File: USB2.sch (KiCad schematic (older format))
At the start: 21 parts

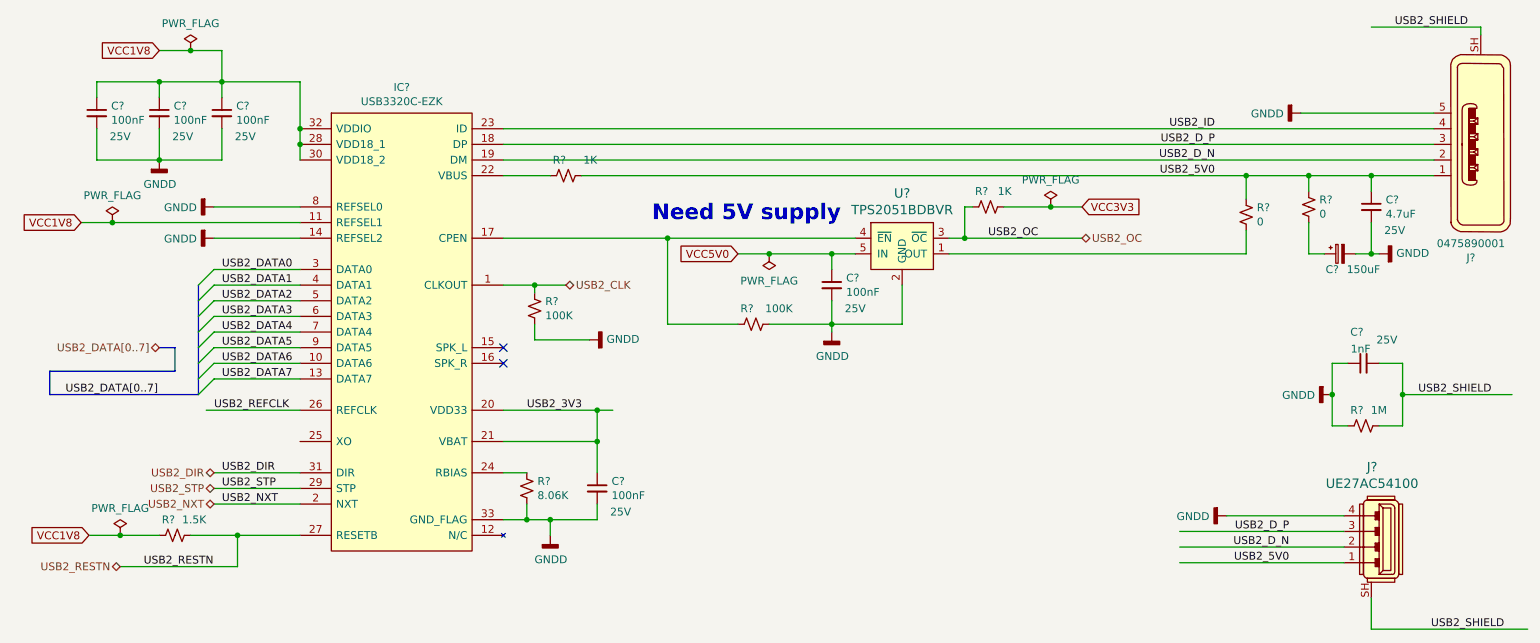
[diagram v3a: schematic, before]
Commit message: PCB created and schematics annotated High speed connections added to the BTB
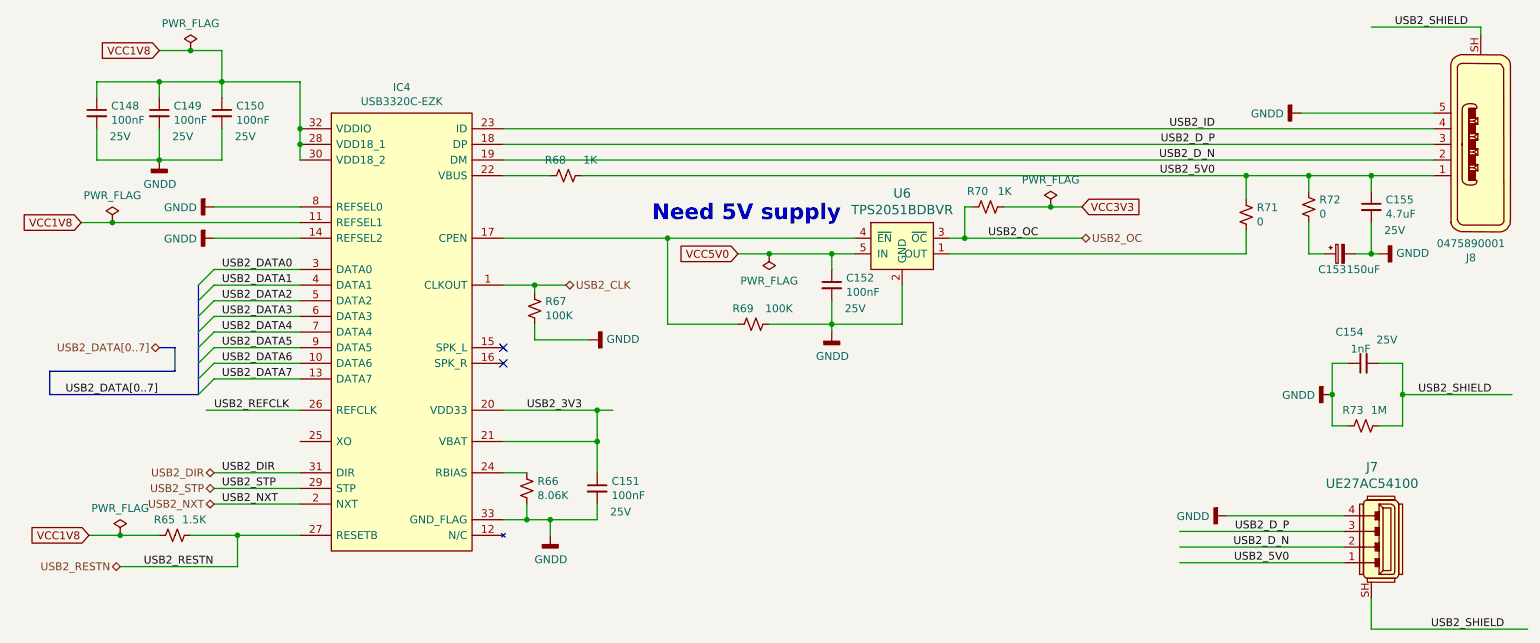
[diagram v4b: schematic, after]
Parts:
- gave numbers to parts that had none: 21

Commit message: Corrected PCB import errors
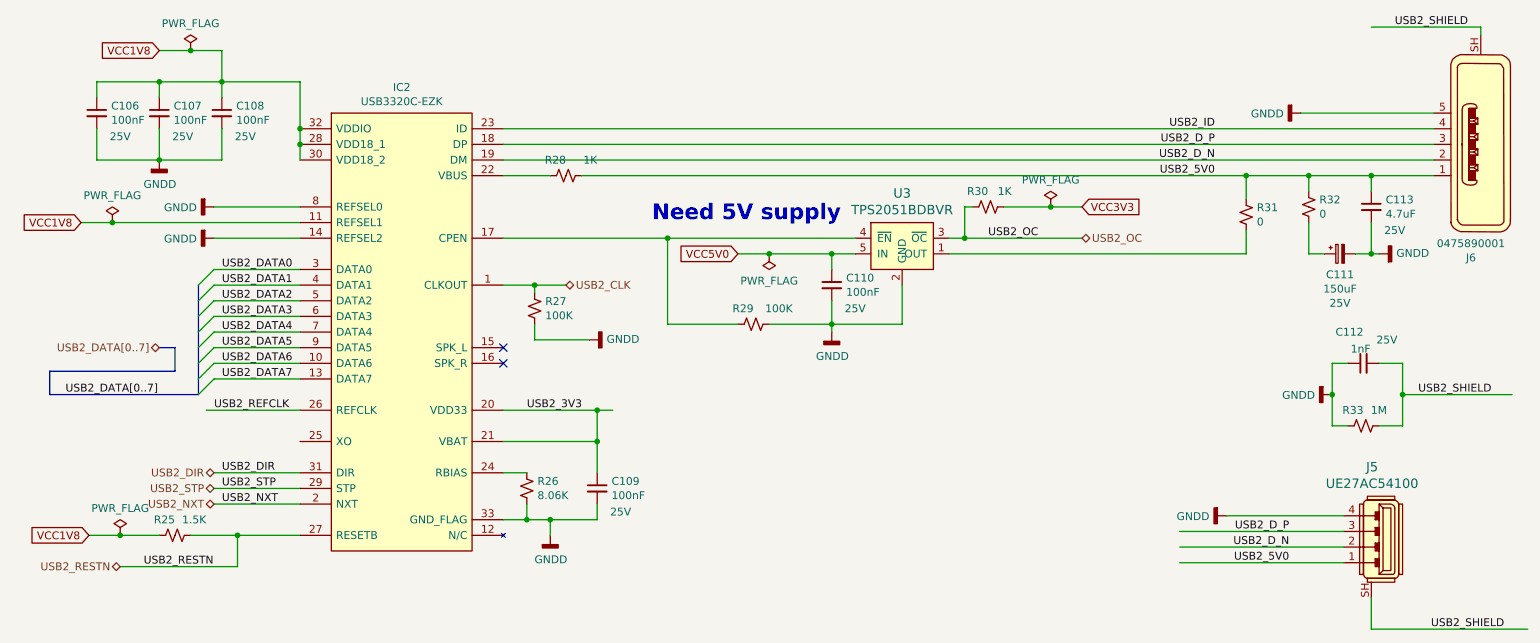
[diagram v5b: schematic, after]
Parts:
- C111: renamed from C153; footprint (none) -> Capacitor_Tantalum_SMD:CP_EIA-7343-30_AVX-N
- renumbered C148 to C106, C149 to C107, C150 to C108, C151 to C109, C152 to C110, C154 to C112, C155 to C113, IC4 to IC2, J7 to J5, J8 to J6, R65 to R25, R66 to R26, R67 to R27, R68 to R28, R69 to R29, R70 to R30, R71 to R31, R72 to R32, R73 to R33, U6 to U3
